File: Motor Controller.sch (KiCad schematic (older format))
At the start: 25 parts, among them P1 Motor_1_in, P10 Motor_3_out, P11 Motor_5_out, P12 Motor_7_out, P13 Motor_2_out, P14 Motor_4_out, P15 Motor_6_out, P16 Motor_8_out, P17 can_bus, P18 Motor_1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

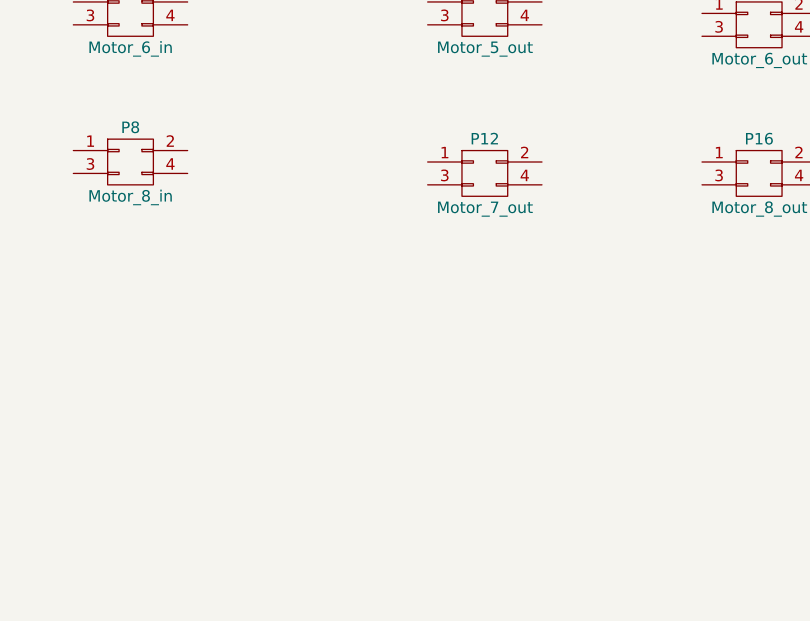
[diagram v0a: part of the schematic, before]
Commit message: Added Led to motor
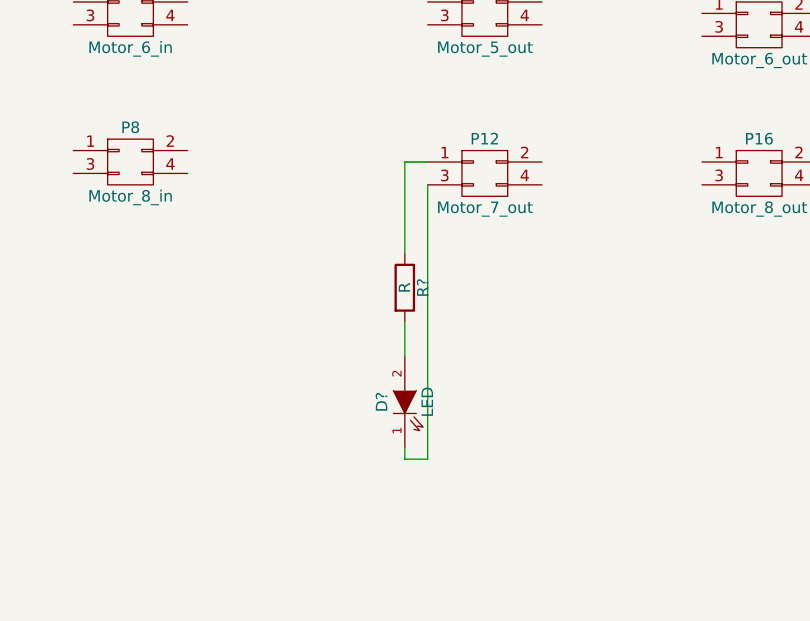
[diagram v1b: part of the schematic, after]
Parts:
- added D?: LED, symbol LED
- added R?: R, symbol R
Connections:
- net at P12.1 (P1): now also R?.1
- net at P12.3 (P3): now also D?.1 (K)
- new net: D?.2 (A), R?.2
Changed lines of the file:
@@
 F1 "Sense_Sheet.sch" 60
 $EndSheet
+$Comp
+L LED D?
+U 1 1 585335DC
+P 3400 4000
+F 0 "D?" H 3400 4100 50  0000 C CNN
+F 1 "LED" H 3400 3900 50  0000 C CNN
+F 2 "" H 3400 4000 50  0000 C CNN
+F 3 "" H 3400 4000 50  0000 C CNN
+	1    3400 4000
+	0    -1   -1   0
+$EndComp
+$Comp
+L R R?
+U 1 1 585337E9
+P 3400 3500
+F 0 "R?" V 3480 3500 50  0000 C CNN
+F 1 "R" V 3400 3500 50  0000 C CNN
+F 2 "" V 3330 3500 50  0000 C CNN
+F 3 "" H 3400 3500 50  0000 C CNN
+	1    3400 3500
+	1    0    0    -1
+$EndComp
+Wire Wire Line
+	3400 3800 3400 3650
+Wire Wire Line
+	3400 4200 3400 4250
+Wire Wire Line
+	3400 3350 3400 2950
+Wire Wire Line
+	3400 2950 3500 2950
+Wire Wire Line
+	3400 4250 3500 4250
+Wire Wire Line
+	3500 4250 3500 3050
 $EndSCHEMATC
